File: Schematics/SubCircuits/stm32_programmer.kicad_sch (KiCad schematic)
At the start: 4 parts, among them J12 Prog edge, J13 Output, SW3 RST

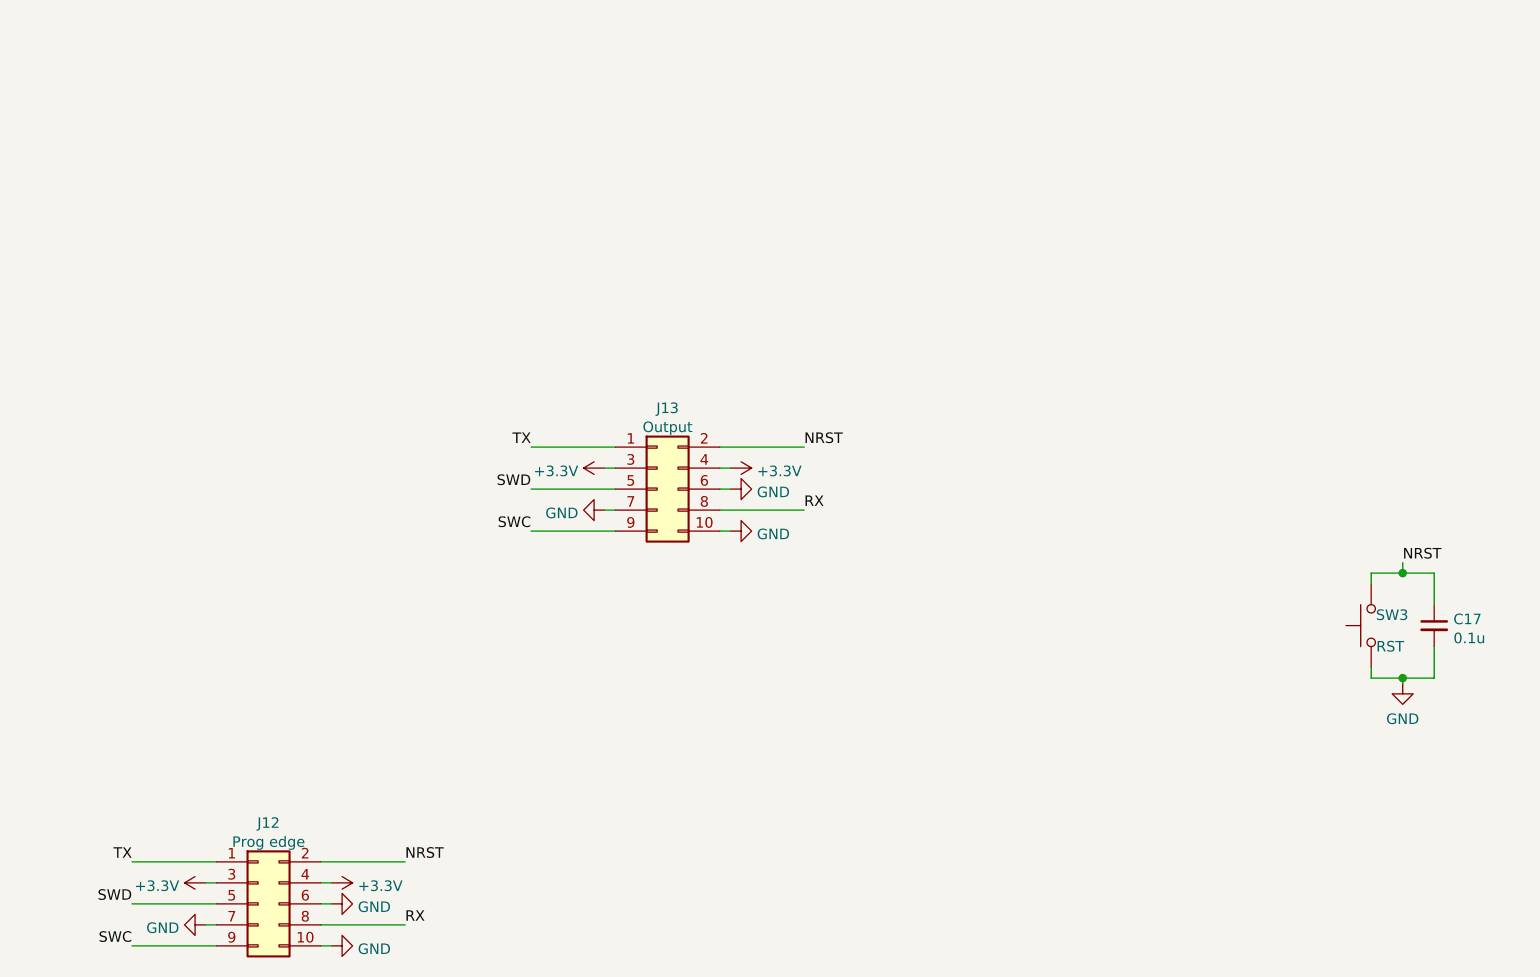
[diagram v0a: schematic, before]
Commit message: Added defunct subcircuit project
superseded by modular mainboard
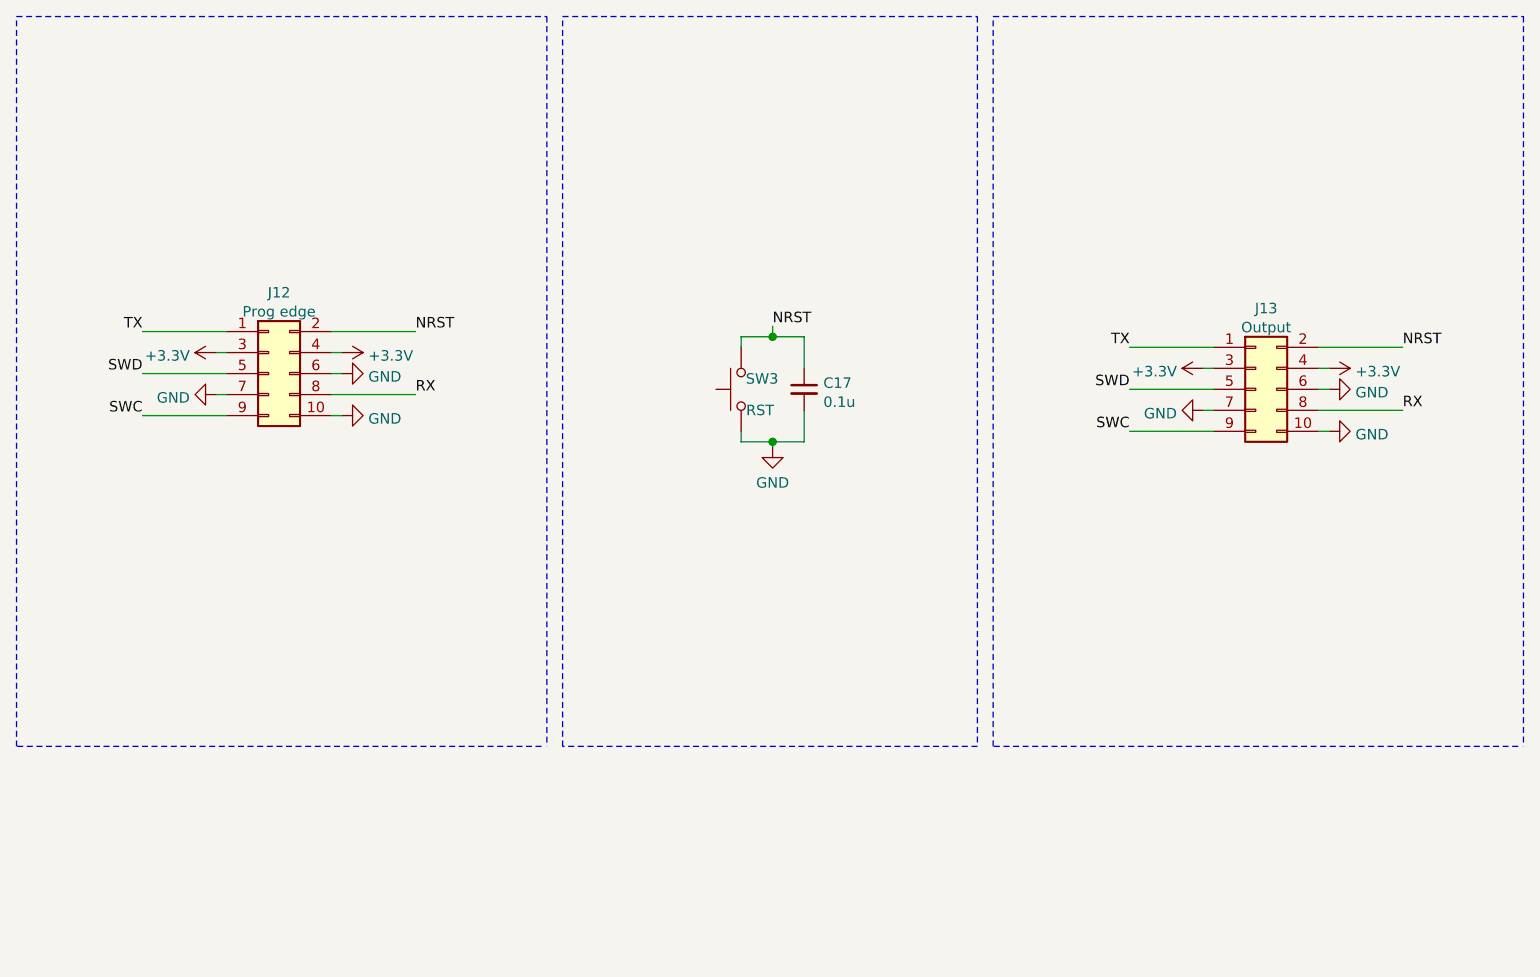
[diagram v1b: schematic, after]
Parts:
- SW3: LCSC Part (none) -> C115357
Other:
- moved on the sheet: C17, J12, J13, SW3
